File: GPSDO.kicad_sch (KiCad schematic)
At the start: 104 parts, among them J1 Conn_Coaxial, J10 Conn_Coaxial, J2 Barrel_Jack, J3 PROG, J4 DISP_MODULE, J5 GPS_CONN, J6 Conn_Coaxial, J7 Conn_Coaxial, J8 Conn_Coaxial, J9 Conn_Coaxial, SW1 RESET_BTN, U1 REF3440IDBVR, U10 LM4040AEX3-3.3+T, U11 AVR32DB28x-xSO, U12 AZ1117H-5.0TRG1, U13 AZ1117H-5.0TRG1, U14 74HC390, U15 DS34C87T, U16 MCP6486T-E/OT, U2 74AUC2G04, U3 74AUC2G04, U4 74LVC2G74DP,125, U5 AD5680, U6 NB3N551MN, U7 74LVC1G125SE-7, U8 74LVC1G125SE-7, U9 LTC2050IS8, X1 OC5SC25

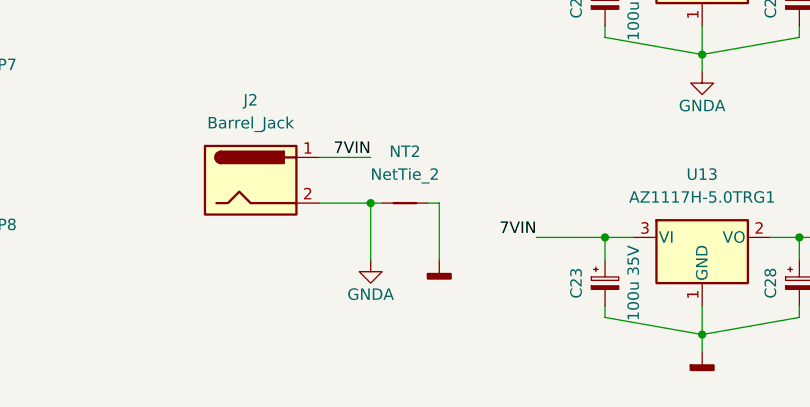
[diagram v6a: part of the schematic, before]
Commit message: Flipped barrel ground: GND and GNDA, added bottom texts
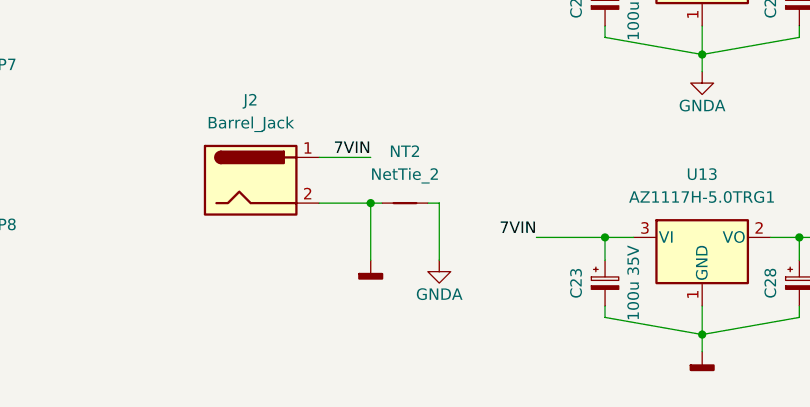
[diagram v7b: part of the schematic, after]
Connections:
- net GND: now also J2.2, NT2.1; no longer NT2.2
- net GNDA: now also NT2.2; no longer J2.2, NT2.1
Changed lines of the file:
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@@
     (pin "1")
   )
-  (symbol (lib_id "power:GNDD") (at 187.325 268.605 0) (unit 1)
-    (in_bom yes) (on_board yes) (fields_autoplaced)
-    (property "Reference" "#PWR065" (id 0) (at 187.325 274.955 0)
-      (effects (font (size 1.27 1.27)) hide)
-    )
-    (property "Value" "GNDD" (id 1) (at 187.325 274.32 0)
-      (effects (font (size 1.27 1.27)) hide)
-    )
-    (property "Footprint" "" (id 2) (at 187.325 268.605 0)
-      (effects (font (size 1.27 1.27)) hide)
-    )
-    (property "Datasheet" "" (id 3) (at 187.325 268.605 0)
+  (symbol (lib_id "power:GNDD") (at 179.705 268.605 0) (unit 1)
+    (in_bom yes) (on_board yes) (fields_autoplaced)
+    (property "Reference" "#PWR065" (id 0) (at 179.705 274.955 0)
+      (effects (font (size 1.27 1.27)) hide)
+    )
+    (property "Value" "GNDD" (id 1) (at 179.705 274.32 0)
+      (effects (font (size 1.27 1.27)) hide)
+    )
+    (property "Footprint" "" (id 2) (at 179.705 268.605 0)
+      (effects (font (size 1.27 1.27)) hide)
+    )
+    (property "Datasheet" "" (id 3) (at 179.705 268.605 0)
       (effects (font (size 1.27 1.27)) hide)
     )
@@
     (pin "2")
   )
-  (symbol (lib_id "power:GNDA") (at 179.705 268.605 0) (unit 1)
-    (in_bom yes) (on_board yes)
-    (property "Reference" "#PWR060" (id 0) (at 179.705 274.955 0)
-      (effects (font (size 1.27 1.27)) hide)
-    )
-    (property "Value" "GNDA" (id 1) (at 179.705 272.415 0))
-    (property "Footprint" "" (id 2) (at 179.705 268.605 0)
-      (effects (font (size 1.27 1.27)) hide)
-    )
-    (property "Datasheet" "" (id 3) (at 179.705 268.605 0)
-      (effects (font (size 1.27 1.27)) hide)
-    )
+  (symbol (lib_id "power:GNDA") (at 187.325 268.605 0) (unit 1)
+    (in_bom yes) (on_board yes)
+    (property "Reference" "#PWR060" (id 0) (at 187.325 274.955 0)
+      (effects (font (size 1.27 1.27)) hide)
+    )
+    (property "Value" "GNDA" (id 1) (at 187.325 272.415 0))
+    (property "Footprint" "" (id 2) (at 187.325 268.605 0)
+      (effects (font (size 1.27 1.27)) hide)
+    )
+    (property "Datasheet" "" (id 3) (at 187.325 268.605 0)
+      (effects (font (size 1.27 1.27)) hide)
+    )
